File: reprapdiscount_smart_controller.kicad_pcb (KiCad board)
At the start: 2 copper layers, 150 x 55 mm, 40 parts, among them Q1 BC817, Q2 BC817, U1 74HC4050, U2 AMS1117-3.3

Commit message: bugfix: switch REVISION var to HASH
Fixes some conflict in the layout
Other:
- board text added: "RepRapDiscount Compatible Smart Controller Revision: ${TAG} (${HASH}) Date: ${DATE}"
- board text removed: "RepRapDiscount Compatible Smart Controller Revision: ${TAG} (${REVISION}) Date: ${DATE}"
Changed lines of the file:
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@@
   )
   (property "DATE" "YYYY-MM-DD HH:MM:SS")
-  (property "REVISION" "REVISION")
+  (property "HASH" "HASH")
   (property "TAG" "TAG")
   (net 0 "")
@@
     (effects (font (size 1 1) (thickness 0.15) bold) (justify left))
   )
-  (gr_text "RepRapDiscount Compatible \nSmart Controller\nRevision: ${TAG} (${REVISION})\nDate: ${DATE}\n" (at 122.1511 125.1036) (layer "F.Mask")
+  (gr_text "RepRapDiscount Compatible \nSmart Controller\nRevision: ${TAG} (${HASH})\nDate: ${DATE}\n" (at 122.1511 125.1036) (layer "F.Mask")
     (effects (font (size 1.5 1.5) (thickness 0.3) bold) (justify left))
   )

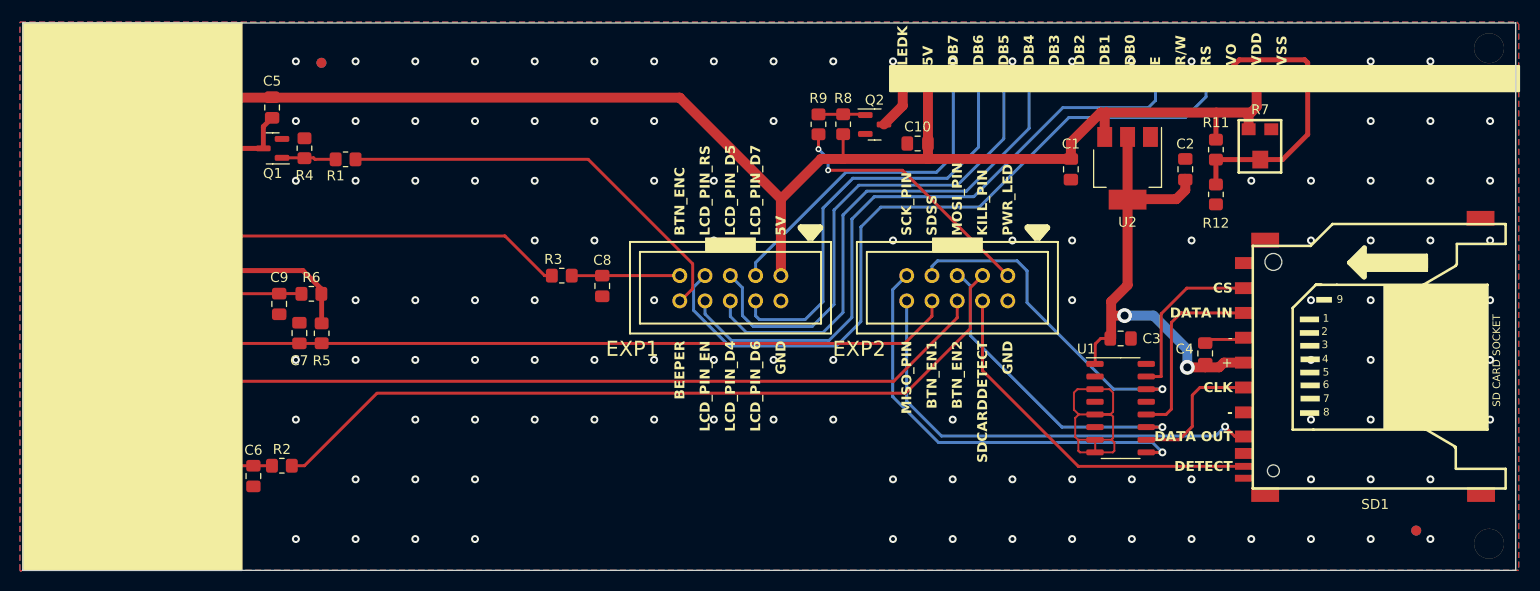
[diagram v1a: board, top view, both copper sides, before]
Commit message: feature: redesign for usb host functionality
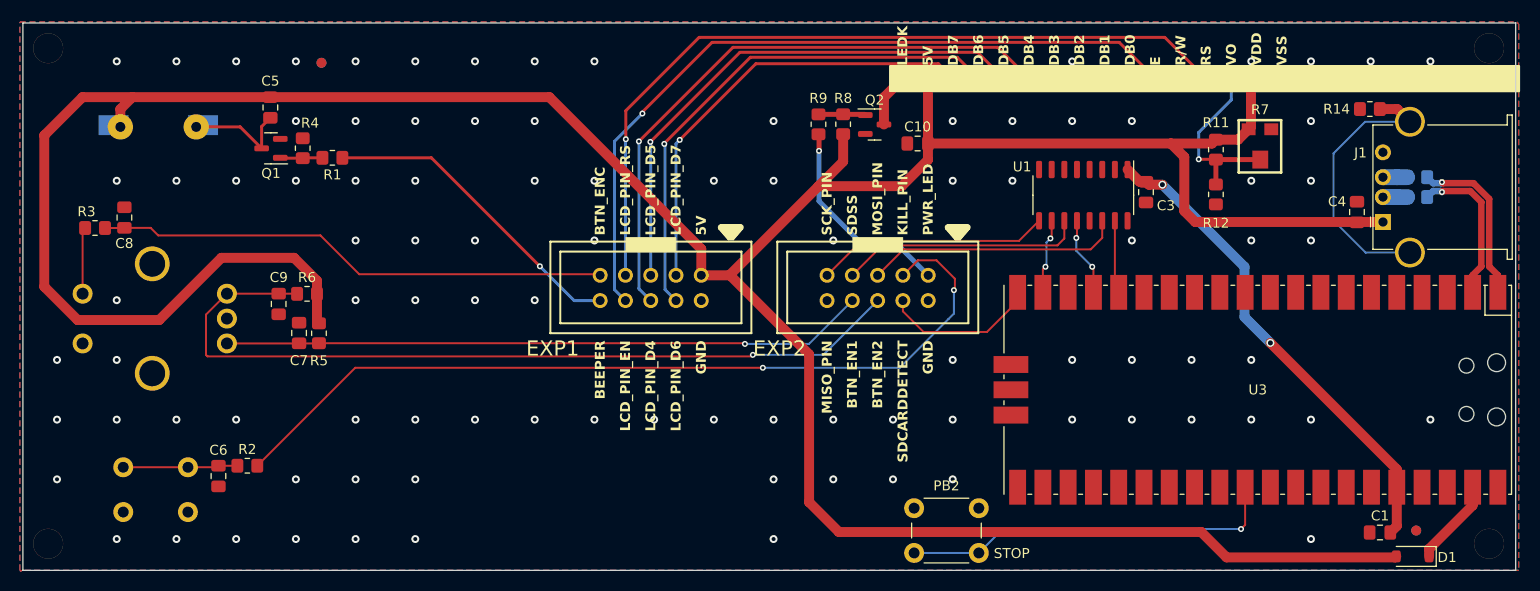
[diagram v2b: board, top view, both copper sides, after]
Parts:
- removed C2: 10u, Capacitor_SMD:C_0805_2012Metric_Pad1.18x1.45mm_HandSolder
- removed SD1: SD card, reprapdiscount_smart_controller:SD_card socket
- removed U2: AMS1117-3.3, Package_TO_SOT_SMD:SOT-223-3_TabPin2
- added D1: MBR120, Diode_SMD:D_SOD-123, F.Cu at (213.2, 131.1)
- added J1: USB_A, Gigahawk:USB_A_Stewart_SS-52100-001_Horizontal, F.Cu at (210.2, 97.5)
- added PB2: STOP, Button_Switch_THT:SW_PUSH_6mm_H7.3mm, F.Cu at (169.6, 130.8)
- added R10: 22R, Resistor_SMD:R_0805_2012Metric_Pad1.20x1.40mm_HandSolder, B.Cu at (213.6, 93.0)
- added R13: 22R, Resistor_SMD:R_0805_2012Metric_Pad1.20x1.40mm_HandSolder, B.Cu at (213.6, 95.0)
- added R14: 0, Resistor_SMD:R_0805_2012Metric_Pad1.20x1.40mm_HandSolder, F.Cu at (208.8, 86.2)
- added U3: Pico, Gigahawk:RPi_Pico_SMD_NO_SILK, F.Cu at (197.6, 114.4)
- moved C8 48.5 mm to (83.7, 97.1), turned to -90 degrees
- moved C1 47.9 mm to (209.9, 128.7), turned to 0 degrees
- moved R3 47.1 mm to (80.8, 98.1)
- moved U1 21.7 mm to (180.1, 94.8), turned to -90 degrees
- moved C4 20.8 mm to (207.6, 96.5)
- moved C3 14.9 mm to (186.3, 94.5), turned to 90 degrees
- moved EXP1 8.00 mm to (126.5, 108.7)
- moved EXP2 8.00 mm to (149.3, 108.7)
- moved C6 3.51 mm to (93.2, 123.0)
- moved R2 3.47 mm to (96.1, 122.0)
- moved R1 1.33 mm to (104.6, 91.0)
- moved R6 0.44 mm to (102.1, 104.7)
- moved R5 0.27 mm to (103.3, 108.7)
- moved C5 0.17 mm to (98.4, 86.0)
- moved Q1 0.17 mm to (98.4, 90.1)
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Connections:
- net /PB1_(SCK) renamed HOST_SCK
- net /RESET renamed RESET
- C1 pad 2: VCC -> +3V3
- C4 pad 2: +3V3 -> VCC
- EXP2 pad 1: /PB3_(MISO) -> SD_MISO
- EXP2 pad 4: /SD_CSEL -> HOST_CS
- EXP2 pad 6: /PB2_(MOSI) -> HOST_MOSI
- U1 pad 10: Net-(SD1-SCLK/CLK) -> SD_SCK
- U1 pad 11: /PB2_(MOSI) -> HOST_CS
- U1 pad 12: Net-(SD1-DI/CMD) -> SD_CS
- U1 pad 14: /SD_CSEL -> HOST_MOSI
- U1 pad 15: Net-(SD1-CS/DAT3) -> SD_MOSI
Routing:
- net VCC: track 205.1 -> 327.4 mm
- net /PB3_(MISO): track 46.2 -> 0.00 mm, vias 1 -> 0
- net Net-(EN1-Pad5): track 51.2 -> 6.70 mm
- net BTN_ENC: track 10.9 -> 51.7 mm
- net PICO_RST: track 0.00 -> 37.9 mm, vias 0 -> 1
- net GND: track 33.9 -> 0.00 mm, vias 135 -> 96
- net /SD_CSEL: track 33.2 -> 0.00 mm, vias 1 -> 0
- net /PB2_(MOSI): track 31.5 -> 0.00 mm, vias 1 -> 0
- net Net-(J1-Shield): track 0.00 -> 28.3 mm
- net HOST_MOSI: track 0.00 -> 25.8 mm
- net HOST_CS: track 0.00 -> 24.6 mm
- net SD_DET: track 37.3 -> 14.7 mm
- net HOST_SCK: track 43.8 -> 23.6 mm, vias 1 -> 0
- net Net-(SD1-DI/CMD): track 18.9 -> 0.00 mm
- net USB_D+: track 0.00 -> 17.9 mm, vias 0 -> 1
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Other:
- board text added: "RepRapDiscount Compatible Smart Controller USB Version Revision: ${TAG} (${HASH}) Date: ${DATE}"
- board text removed: "+"
- board text removed: "-"
- board text removed: "1"
- board text removed: "2"
- board text removed: "3"
- board text removed: "4"
- board text removed: "5"
- board text removed: "6"
- board text removed: "7"
- board text removed: "8"
- board text removed: "9"
- board text removed: "CLK"
- board text removed: "CS"
- board text removed: "DATA IN"
- board text removed: "DATA OUT"
- board text removed: "DETECT"
- board text removed: "Data IN"
- board text removed: "Data OUT"
- board text removed: "Data1"
- board text removed: "Data2"
- board text removed: "RepRapDiscount Compatible Smart Controller Revision: ${TAG} (${HASH}) Date: ${DATE}"
- board text removed: "SD CARD SOCKET"
- board text removed: "VSS1"
- board text removed: "VSS2"

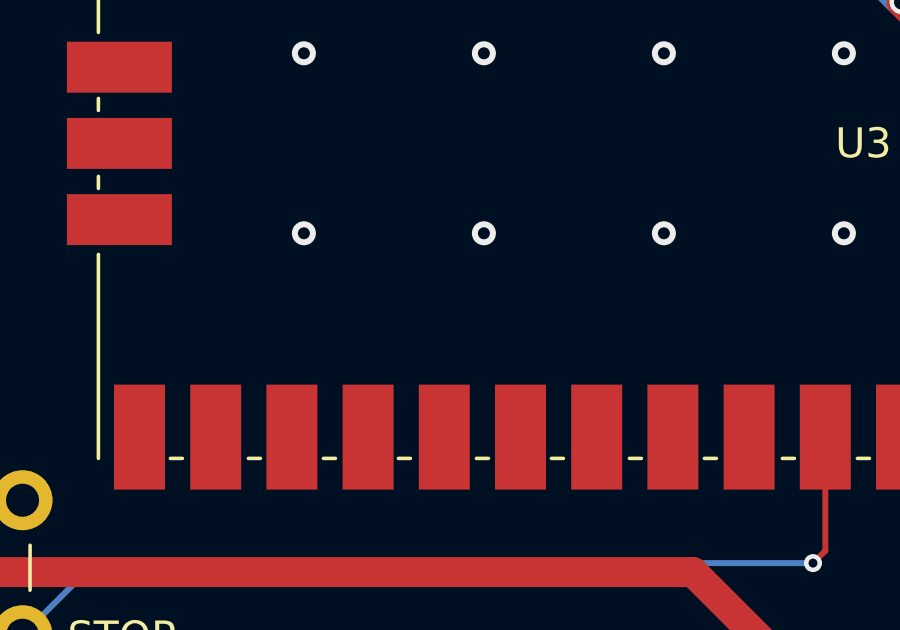
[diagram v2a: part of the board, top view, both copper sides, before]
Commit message: feature: add order number location
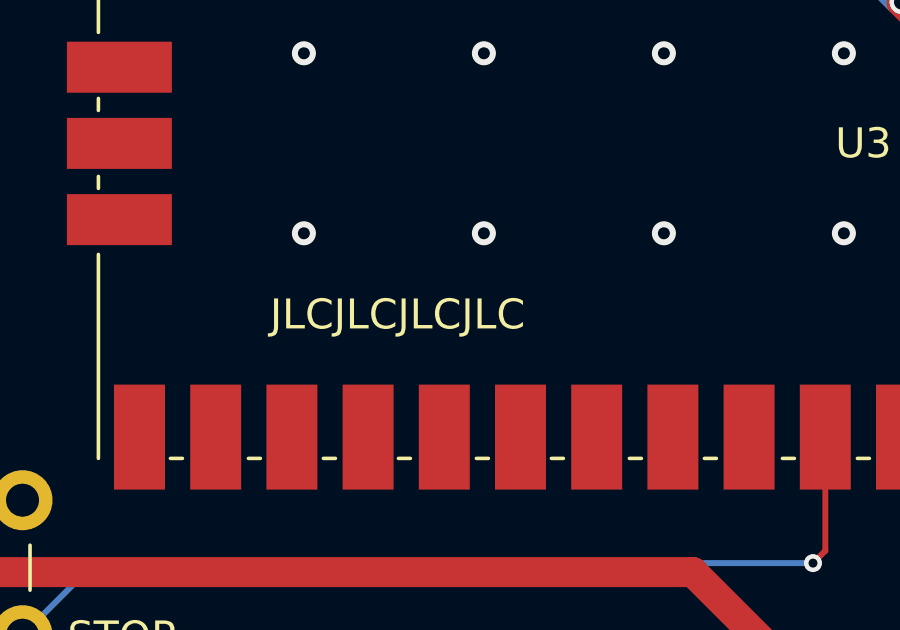
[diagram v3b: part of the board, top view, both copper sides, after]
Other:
- board text added: "JLCJLCJLCJLC"
- board text added: "Manufacture at JLCPCB, 1.6mm thickness"
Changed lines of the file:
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@@
     (effects (font (size 1 1) (thickness 0.15) bold) (justify left))
+  )
+  (gr_text "JLCJLCJLCJLC" (at 177.8 120.65) (layer "F.SilkS")
+    (effects (font (size 1 1) (thickness 0.15)) (justify left bottom))
   )
   (gr_text "BTN_ENC" (at 131.5011 98.8536 90) (layer "F.SilkS")
@@
     (effects (font (size 1.5 1.5) (thickness 0.3) bold) (justify left))
   )
+  (gr_text "Manufacture at JLCPCB, 1.6mm thickness" (at 186.69 139.7) (layer "Cmts.User")
+    (effects (font (size 1 1) (thickness 0.15)) (justify left bottom))
+  )
   (segment (start 191.65 91.2) (end 193.3475 91.2) (width 0.3) (layer "F.Cu") (net 1))

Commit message: layout: slight adjustments to layout
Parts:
- PB2: value STOP -> PICO_RST
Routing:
- net BTN_EN1: track 83.9 -> 86.5 mm
- net LCDRS: track 79.6 -> 79.0 mm
- net GND: vias 96 -> 97

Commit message: layout: minor fixes and adjustments
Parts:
- PB2: value PICO_RST -> STOP
- moved C5 3.87 mm to (94.5, 86.0)
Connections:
- U3 pad 15: unconnected-(U3-GPIO11-Pad15) -> SD_MISO
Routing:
- net SD_MISO: track 0.00 -> 34.8 mm
- net VCC: track 327.5 -> 329.8 mm
- net Net-(PZ1-+): track 10.9 -> 8.73 mm
- net GND: vias 97 -> 96

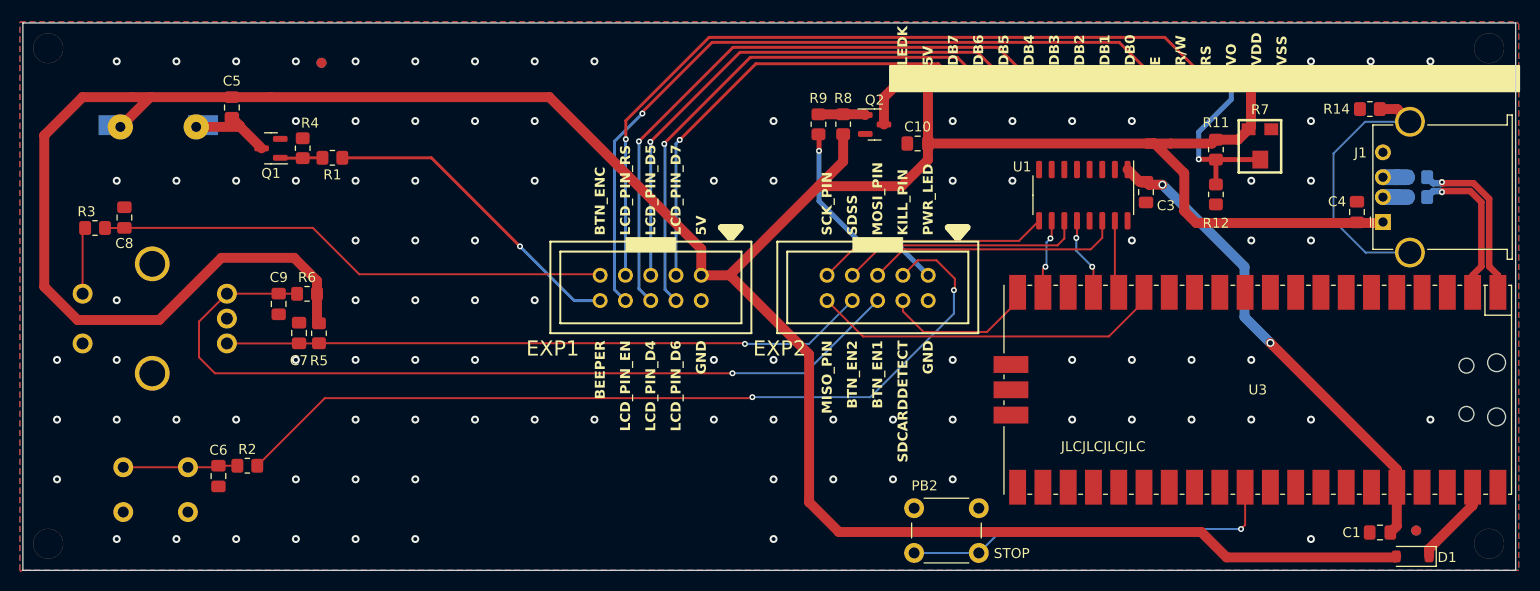
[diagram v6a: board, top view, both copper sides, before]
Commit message: feature: add status leds to pico
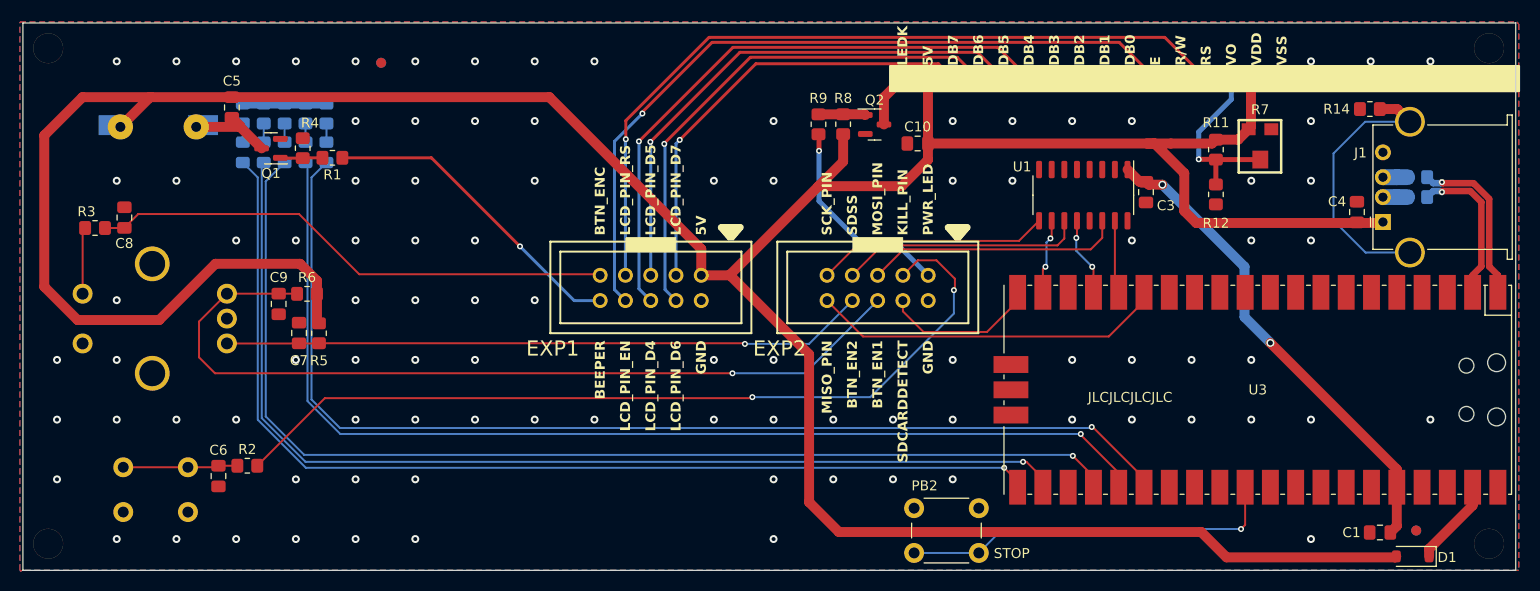
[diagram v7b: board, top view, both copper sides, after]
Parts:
- added D2: RED, LED_SMD:LED_0805_2012Metric_Pad1.15x1.40mm_HandSolder, B.Cu at (104.0, 90.5)
- added D3: GRN, LED_SMD:LED_0805_2012Metric_Pad1.15x1.40mm_HandSolder, B.Cu at (101.9, 90.5)
- added D4: BLU, LED_SMD:LED_0805_2012Metric_Pad1.15x1.40mm_HandSolder, B.Cu at (99.8, 90.5)
- added D5: YLW, LED_SMD:LED_0805_2012Metric_Pad1.15x1.40mm_HandSolder, B.Cu at (97.7, 90.5)
- added D6: WHT, LED_SMD:LED_0805_2012Metric_Pad1.15x1.40mm_HandSolder, B.Cu at (95.6, 90.5)
- added R15: 1k, Resistor_SMD:R_0805_2012Metric_Pad1.20x1.40mm_HandSolder, B.Cu at (104.0, 86.6)
- added R16: 1k, Resistor_SMD:R_0805_2012Metric_Pad1.20x1.40mm_HandSolder, B.Cu at (101.9, 86.6)
- added R17: 1k, Resistor_SMD:R_0805_2012Metric_Pad1.20x1.40mm_HandSolder, B.Cu at (99.8, 86.6)
- added R18: 1k, Resistor_SMD:R_0805_2012Metric_Pad1.20x1.40mm_HandSolder, B.Cu at (97.7, 86.6)
- added R19: 1k, Resistor_SMD:R_0805_2012Metric_Pad1.20x1.40mm_HandSolder, B.Cu at (95.6, 86.6)
- moved FID1 6.00 mm to (109.5, 81.5)
- moved FID4 6.00 mm to (109.5, 81.5)
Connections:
- U3 pad 21: unconnected-(U3-GPIO16-Pad21) -> LED5
- U3 pad 22: unconnected-(U3-GPIO17-Pad22) -> LED4
- U3 pad 24: unconnected-(U3-GPIO18-Pad24) -> LED3
- U3 pad 25: unconnected-(U3-GPIO19-Pad25) -> LED2
- U3 pad 26: unconnected-(U3-GPIO20-Pad26) -> LED1
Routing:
- net LED3: track 0.00 -> 112.1 mm, vias 0 -> 1
- net LED1: track 0.00 -> 111.4 mm, vias 0 -> 1
- net LED2: track 0.00 -> 109.3 mm, vias 0 -> 1
- net LED4: track 0.00 -> 106.8 mm, vias 0 -> 1
- net LED5: track 0.00 -> 105.2 mm, vias 0 -> 1
- net GND: track 0.00 -> 8.40 mm, vias 96 -> 95
- net Net-(D6-K): track 0.00 -> 1.88 mm
- net Net-(D5-K): track 0.00 -> 1.88 mm
- net Net-(D4-K): track 0.00 -> 1.88 mm
- net Net-(D3-K): track 0.00 -> 1.88 mm
- net Net-(D2-K): track 0.00 -> 1.88 mm
- net BTN_ENC: track 51.7 -> 52.9 mm

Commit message: feature: use buffer to drive leds
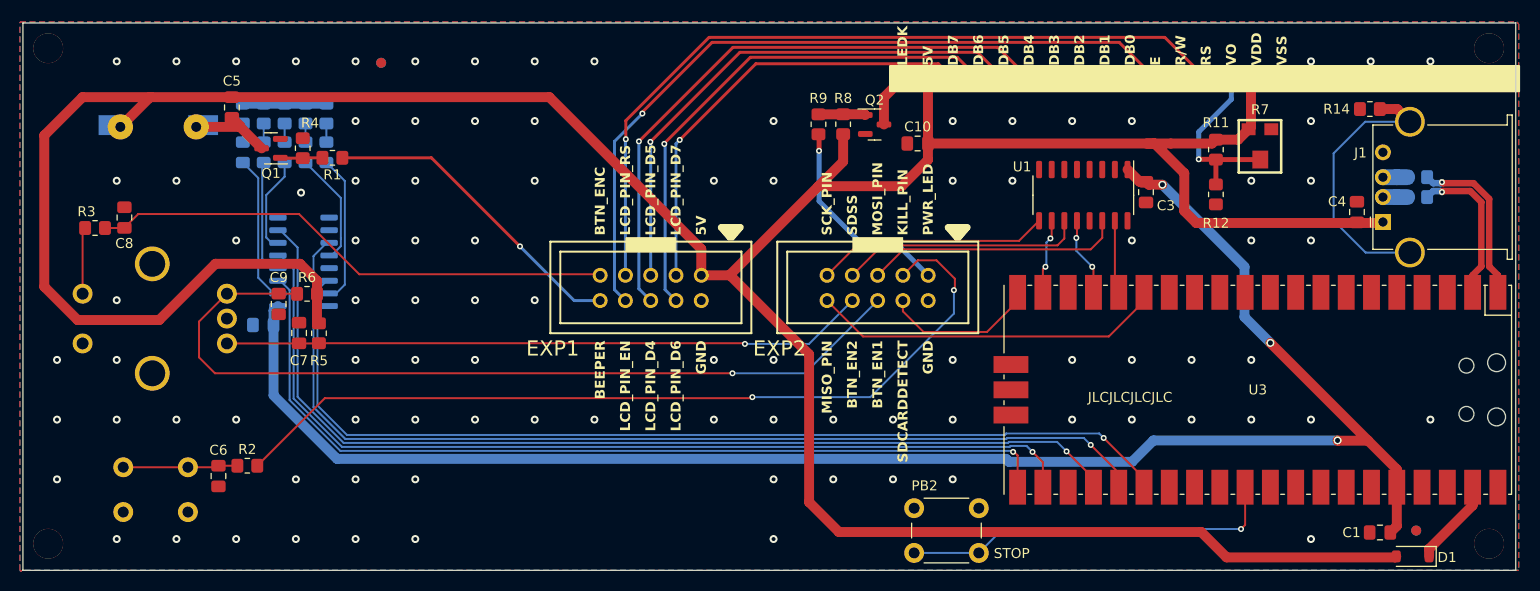
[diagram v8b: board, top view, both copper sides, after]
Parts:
- added C2: 100n, Capacitor_SMD:C_0805_2012Metric_Pad1.18x1.45mm_HandSolder, B.Cu at (97.7, 107.8)
- added U2: 74HC4050, reprapdiscount_smart_controller:SO-16_3.9x9.9mm_P1.27mm, B.Cu at (101.7, 101.5)
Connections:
- D2 pad 2: LED1 -> Net-(D2-A)
- D3 pad 2: LED2 -> Net-(D3-A)
- D4 pad 2: LED3 -> Net-(D4-A)
- D5 pad 2: LED4 -> Net-(D5-A)
- D6 pad 2: LED5 -> Net-(D6-A)
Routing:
- net +3V3: track 49.1 -> 171.9 mm, vias 2 -> 3
- net Net-(D2-A): track 0.00 -> 15.0 mm
- net LED5: track 105.2 -> 90.4 mm
- net Net-(D6-A): track 0.00 -> 14.8 mm
- net LED1: track 111.4 -> 99.4 mm
- net LED4: track 106.8 -> 94.8 mm
- net Net-(D3-A): track 0.00 -> 11.9 mm
- net Net-(D5-A): track 0.00 -> 11.7 mm
- net LED3: track 112.1 -> 101.1 mm
- net Net-(D4-A): track 0.00 -> 9.69 mm
- net LED2: track 109.3 -> 101.6 mm
- net GND: vias 95 -> 94
